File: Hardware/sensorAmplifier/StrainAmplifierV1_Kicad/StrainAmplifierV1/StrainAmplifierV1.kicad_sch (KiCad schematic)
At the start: 13 parts, among them U1 INA333AIDGKR, U2 TLV9061SQDBVRQ1

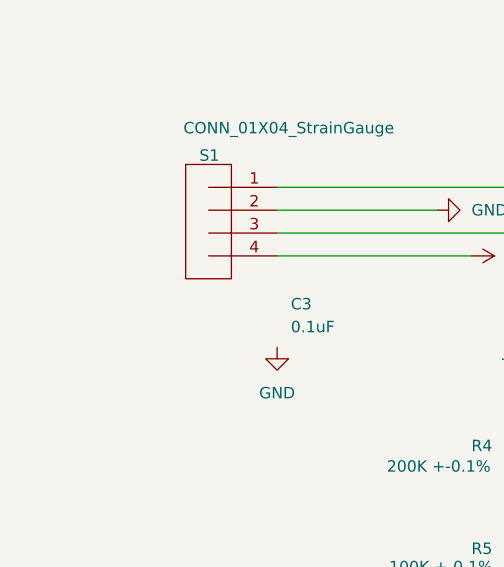
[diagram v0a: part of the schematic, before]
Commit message: Documentation files on LTSPICE stimulations, as well as RC FILTER created
LTSPICE stimulations
	ALL circuits restimulated, documented in test folder
RC FILTER calculations which filters out a lot of noise concerns.
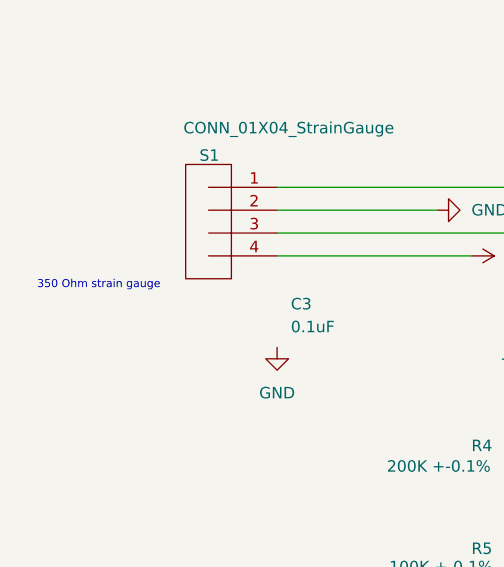
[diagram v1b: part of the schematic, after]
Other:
- note added: "350 Ohm strain gauge"
